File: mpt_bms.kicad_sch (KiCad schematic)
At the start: 33 parts, among them Q2 BSS138, U2 BQ25185, U3 BQ27441-G1, U6 TPS63031

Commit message: Added Info-Table for STAT Pins and LEDS of Charger Work In Progress regulation for Display driving (currently not working)
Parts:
- removed R29: 10k, passive:R_0603, symbol db:resistor_0603/00.018.0009.0046
- added R27: 196k, passive:R_0603, symbol db:resistor_0603/00.018.0009.0244
- added R28: 1M15, passive:R_0603, symbol db:resistor_0603/00.018.0009.0091
- added R29: 100k, passive:R_0603, symbol db:resistor_0603/00.018.0009.0047
- U6: value TPS63031 -> TPS63030; symbol db:power_ic/11.015.0044.0002 -> db:power_ic/11.015.0044.0003; Dist1# digikey -> 296-39460-1-ND; MFR# TPS63031DSKR -> TPS63030DSKR; Modified 2026-10-09 11:42:52 -> 2026-10-10 20:29:52
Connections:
- net GND: now also R27.2, R29.2
- net at Q2.1 (G), R30.1: now also R29.1
- net +3V3 renamed +3V4
- net +3V4: now also R28.1; no longer U6.10 (FB)
- new net: R27.1, R28.2, U6.10 (FB)
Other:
- moved on the sheet: BT1, BT2, C11, C12, C13, C14, C2, C4, C6, C7, C8, D1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

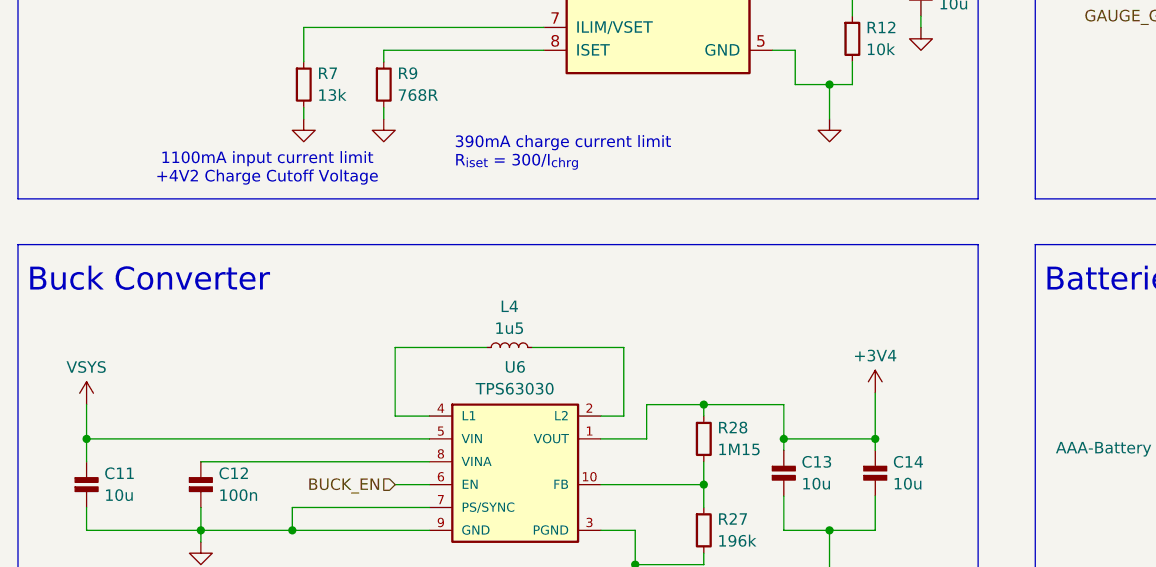
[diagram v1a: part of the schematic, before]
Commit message: Changed LED Driver for one with lower Headroom
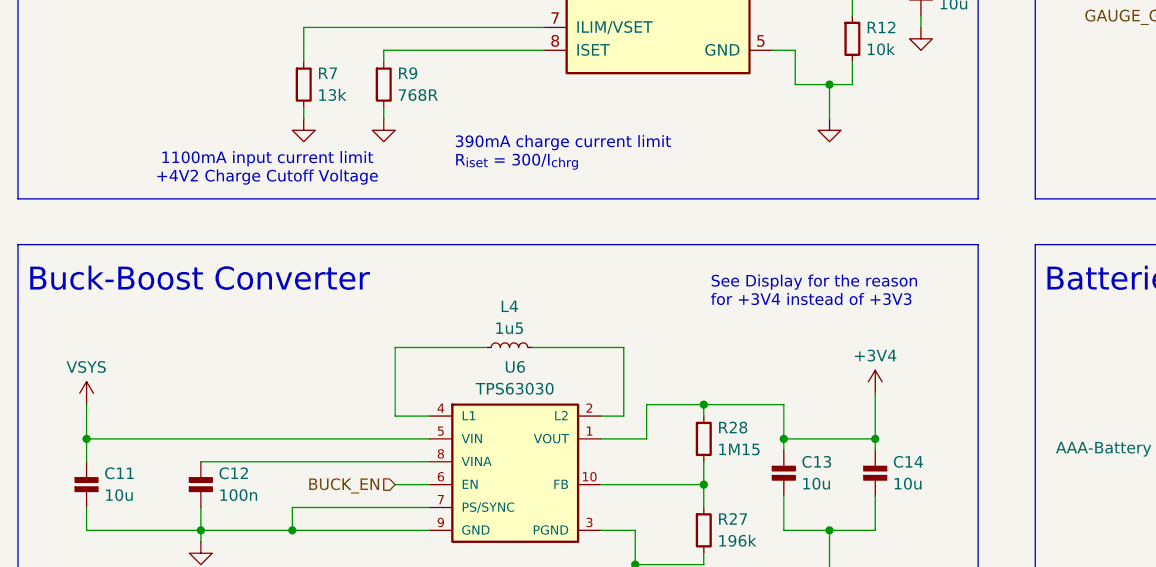
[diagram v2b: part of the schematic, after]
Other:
- note added: "Buck-Boost Converter"
- note added: "See Display for the reason for +3V4 instead of +3V3"
- note removed: "Buck Converter"
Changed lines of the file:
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@@
 		)
 	)
-	(text "Buck Converter"
+	(text "Buck-Boost Converter"
 		(exclude_from_sim no)
 		(at 41.656 82.804 0)
@@
 			)
 			(justify left)
+		)
+	)
+	(text "See Display for the reason \nfor +3V4 instead of +3V3"
+		(exclude_from_sim no)
+		(at 117.602 84.074 0)
+		(effects
+			(font
+				(size 1.27 1.27)
+			)
+			(justify left)

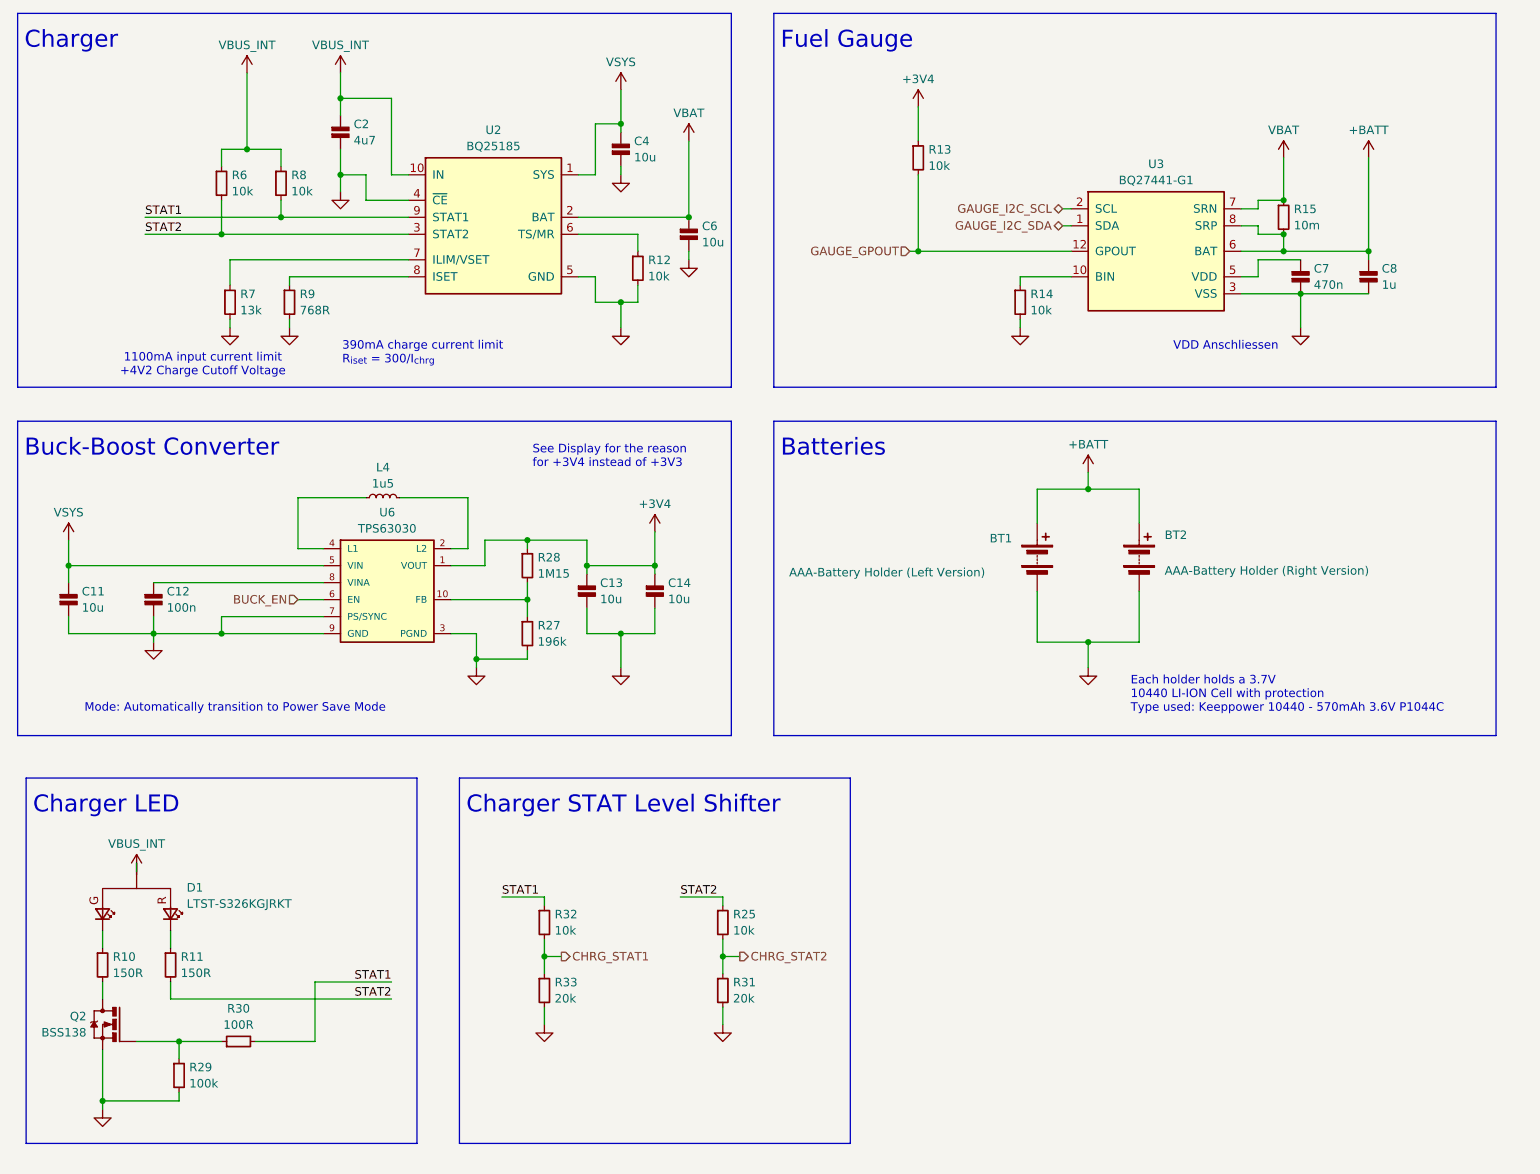
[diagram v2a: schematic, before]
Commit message: Updated PCB Layout with new Buck Boost, Display driver and STAT Led logic
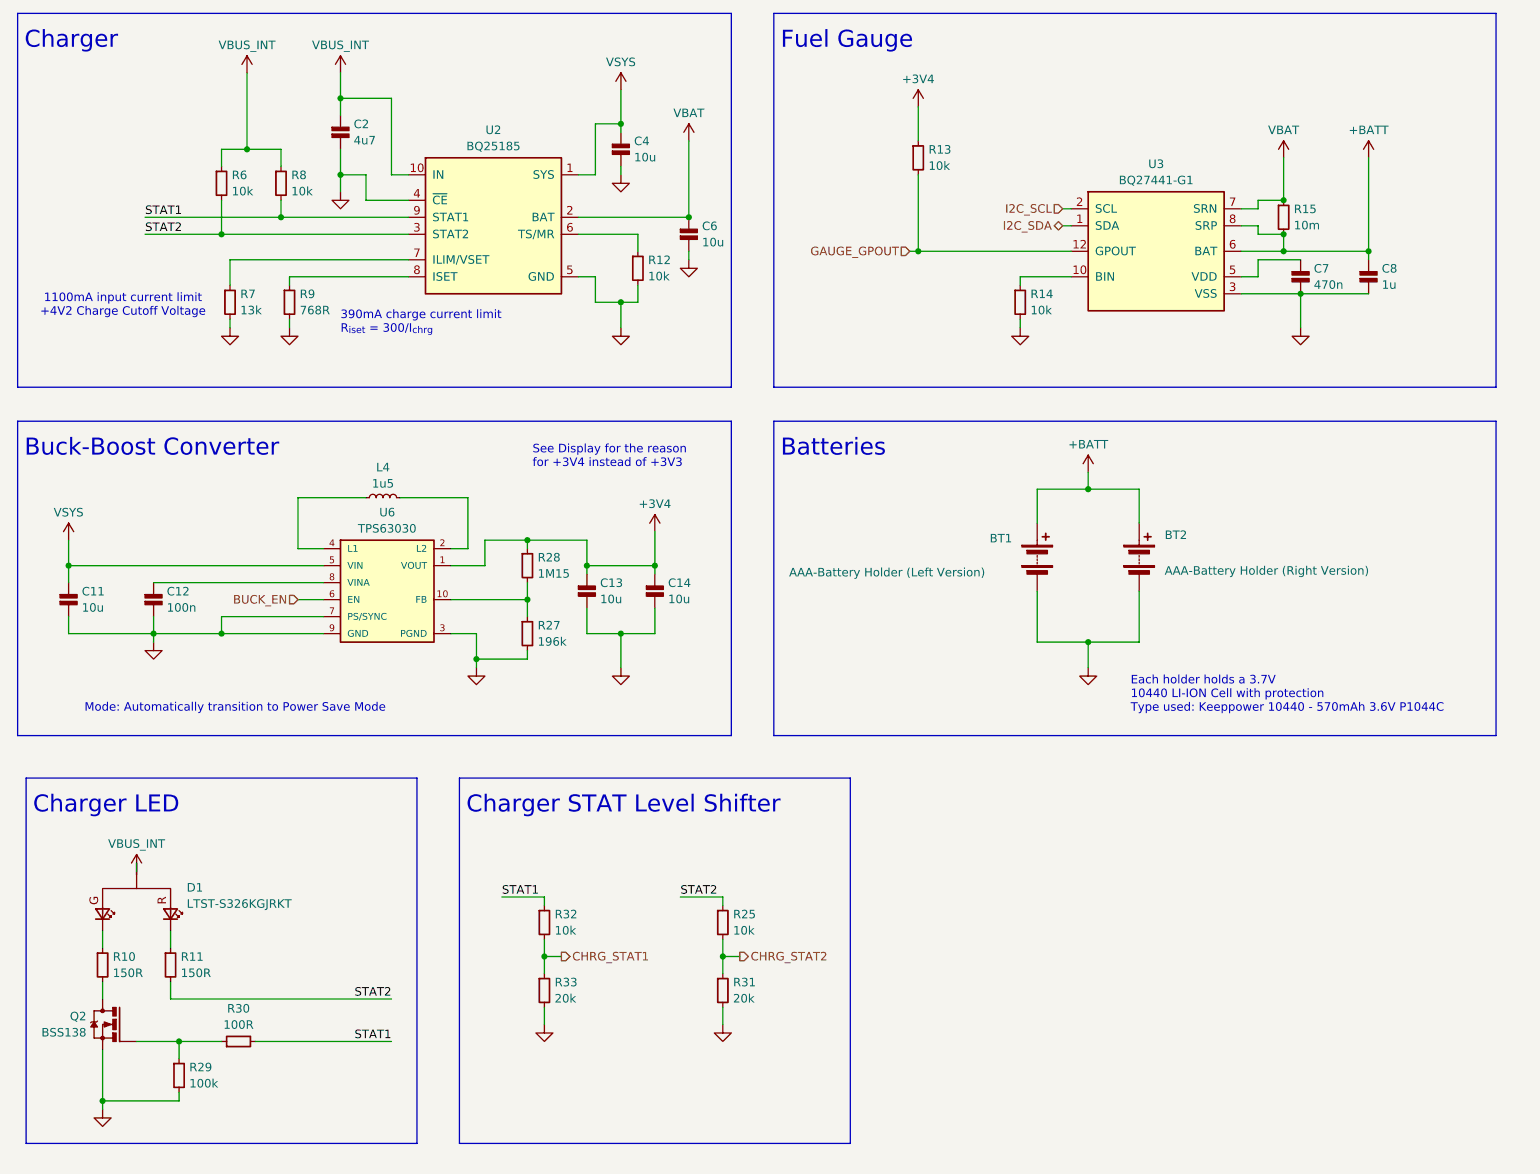
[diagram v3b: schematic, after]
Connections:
- net at R10.1: now also D1.3 (C_G); no longer D1.4 (C_G)
- net GAUGE_I2C_SCL renamed I2C_SCL
- net GAUGE_I2C_SDA renamed I2C_SDA
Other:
- note removed: "VDD Anschliessen"

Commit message: Make Block Titles consistent in size Remove not connected marks on mcu for pins which can be used for user buttons and other stuff Add User button hierarchy lables for Button 4 & 5 on MCU sheet Fix hierarchichal pin names on the block not matching the sheet
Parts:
- L4: footprint passive:L_Coilcraft_LPS301X -> passive:L_2.5mmx1.9mm; symbol db:inductor/02.045.0052.0001 -> db:inductor/02.002.0006.0002; Dist1 mouser -> digikey; Dist1# 994-LPS3015-152MRC -> 118-SRP2010TMA-1R5MCT-ND; Dist2 none -> mouser; Dist2# (none) -> 652-SRP2010TMA-1R5M; FP L_Coilcraft_LPS301X -> L_2.5mmx1.9mm; MFR Coilcraft -> Bourns; MFR# LPS3015-152MRC -> SRP2010TMA-1R5M; Modified 2026-10-09 12:16:53 -> 2026-10-15 11:43:07; Rating 20% 100mOhms -> 2A6, 20%, 80mOhm; Series LPS -> SRP3212
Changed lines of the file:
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@@
 		(title "M.P.T BMS")
 		(company "Hochschule Luzern, Technik & Architektur")
+		(comment 1 "Designed by Nico Theiler & Dominik Grob")
 	)
 	(rectangle
@@
 	)
 	(symbol
-		(lib_id "db:inductor/02.045.0052.0001")
+		(lib_id "db:inductor/02.002.0006.0002")
 		(at 95.25 90.17 90)
 		(unit 1)
@@
 			)
 		)
-		(property "Footprint" "passive:L_Coilcraft_LPS301X"
+		(property "Footprint" "passive:L_2.5mmx1.9mm"
 			(at 95.25 90.17 0)
 			(hide yes)
@@
 			)
 		)
-		(property "Datasheet" "${KICAD_USER_DATASHEET_DIR}passive/DS_Coilcraft_LPS3015.pdf"
+		(property "Datasheet" "${KICAD_USER_DATASHEET_DIR}\\passive\\DS_BOURNS_SRP2010TMA.pdf"
 			(at 95.25 90.17 0)
 			(hide yes)
@@
 			)
 		)
-		(property "Description" "Power Inductor"
+		(property "Description" "Shielded Power Inductor"
 			(at 95.25 90.17 0)
 			(hide yes)
@@
 			)
 		)
-		(property "MFR" "Coilcraft"
+		(property "MFR" "Bourns"
 			(at 95.25 90.17 0)
 			(hide yes)
@@
 			)
 		)
-		(property "Series" "LPS"
+		(property "Series" "SRP3212"
 			(at 95.25 90.17 0)
 			(hide yes)
@@
 			)
 		)
-		(property "MFR#" " LPS3015-152MRC "
+		(property "MFR#" "SRP2010TMA-1R5M"
 			(at 95.25 90.17 0)
 			(hide yes)
@@
 			)
 		)
-		(property "Rating" "20% 100mOhms"
+		(property "Rating" "2A6, 20%, 80mOhm"
 			(at 95.25 90.17 0)
 			(hide yes)
@@
 			)
 		)
-		(property "Dist1" "mouser"
+		(property "Dist1" "digikey"
 			(at 95.25 90.17 0)
 			(hide yes)
@@
 			)
 		)
-		(property "Dist1#" "994-LPS3015-152MRC"
+		(property "Dist1#" "118-SRP2010TMA-1R5MCT-ND"
 			(at 95.25 90.17 0)
 			(hide yes)
@@
 			)
 		)
-		(property "Dist2" "none"
+		(property "Dist2" "mouser"
 			(at 95.25 90.17 0)
 			(hide yes)
@@
 			)
 		)
-		(property "Dist2#" ""
+		(property "Dist2#" " 652-SRP2010TMA-1R5M "
 			(at 95.25 90.17 0)
 			(hide yes)
@@
 			)
 		)
-		(property "Modified" "2026-10-09 12:16:53"
+		(property "Modified" "2026-10-15 11:43:07"
 			(at 95.25 90.17 0)
 			(hide yes)
@@
 			)
 		)
-		(property "FP" "L_Coilcraft_LPS301X"
+		(property "FP" "L_2.5mmx1.9mm"
 			(at 95.25 90.17 0)
 			(hide yes)
